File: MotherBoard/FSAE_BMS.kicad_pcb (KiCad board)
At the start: 4 copper layers, 139.7 x 127 mm, 209 parts, among them IC501 BQ79600PWRQ1, J201 Conn_ARM_SWD_TagConnect_TC2030, J202 DM3AT-SF-PEJM5_40_, J301 1376357-3, J302 Conn_01x04_Pin, J303 430450200, Q701 Q_NMOS_GDS, Q702 Q_NPN_BEC, Q703 Q_NPN_BEC, Q704 Q_NMOS_GDS, Q705 Q_NPN_BEC, Q706 Q_NMOS_GDS, Q708 Q_NPN_BEC, Q709 Q_NMOS_GDS, U201 STM32F205RBTx, U401 LMR51430, U402 LMR51430, U601 PTCAN1462DRQ1, U602 PTCAN1462DRQ1, Y201 16 Mhz

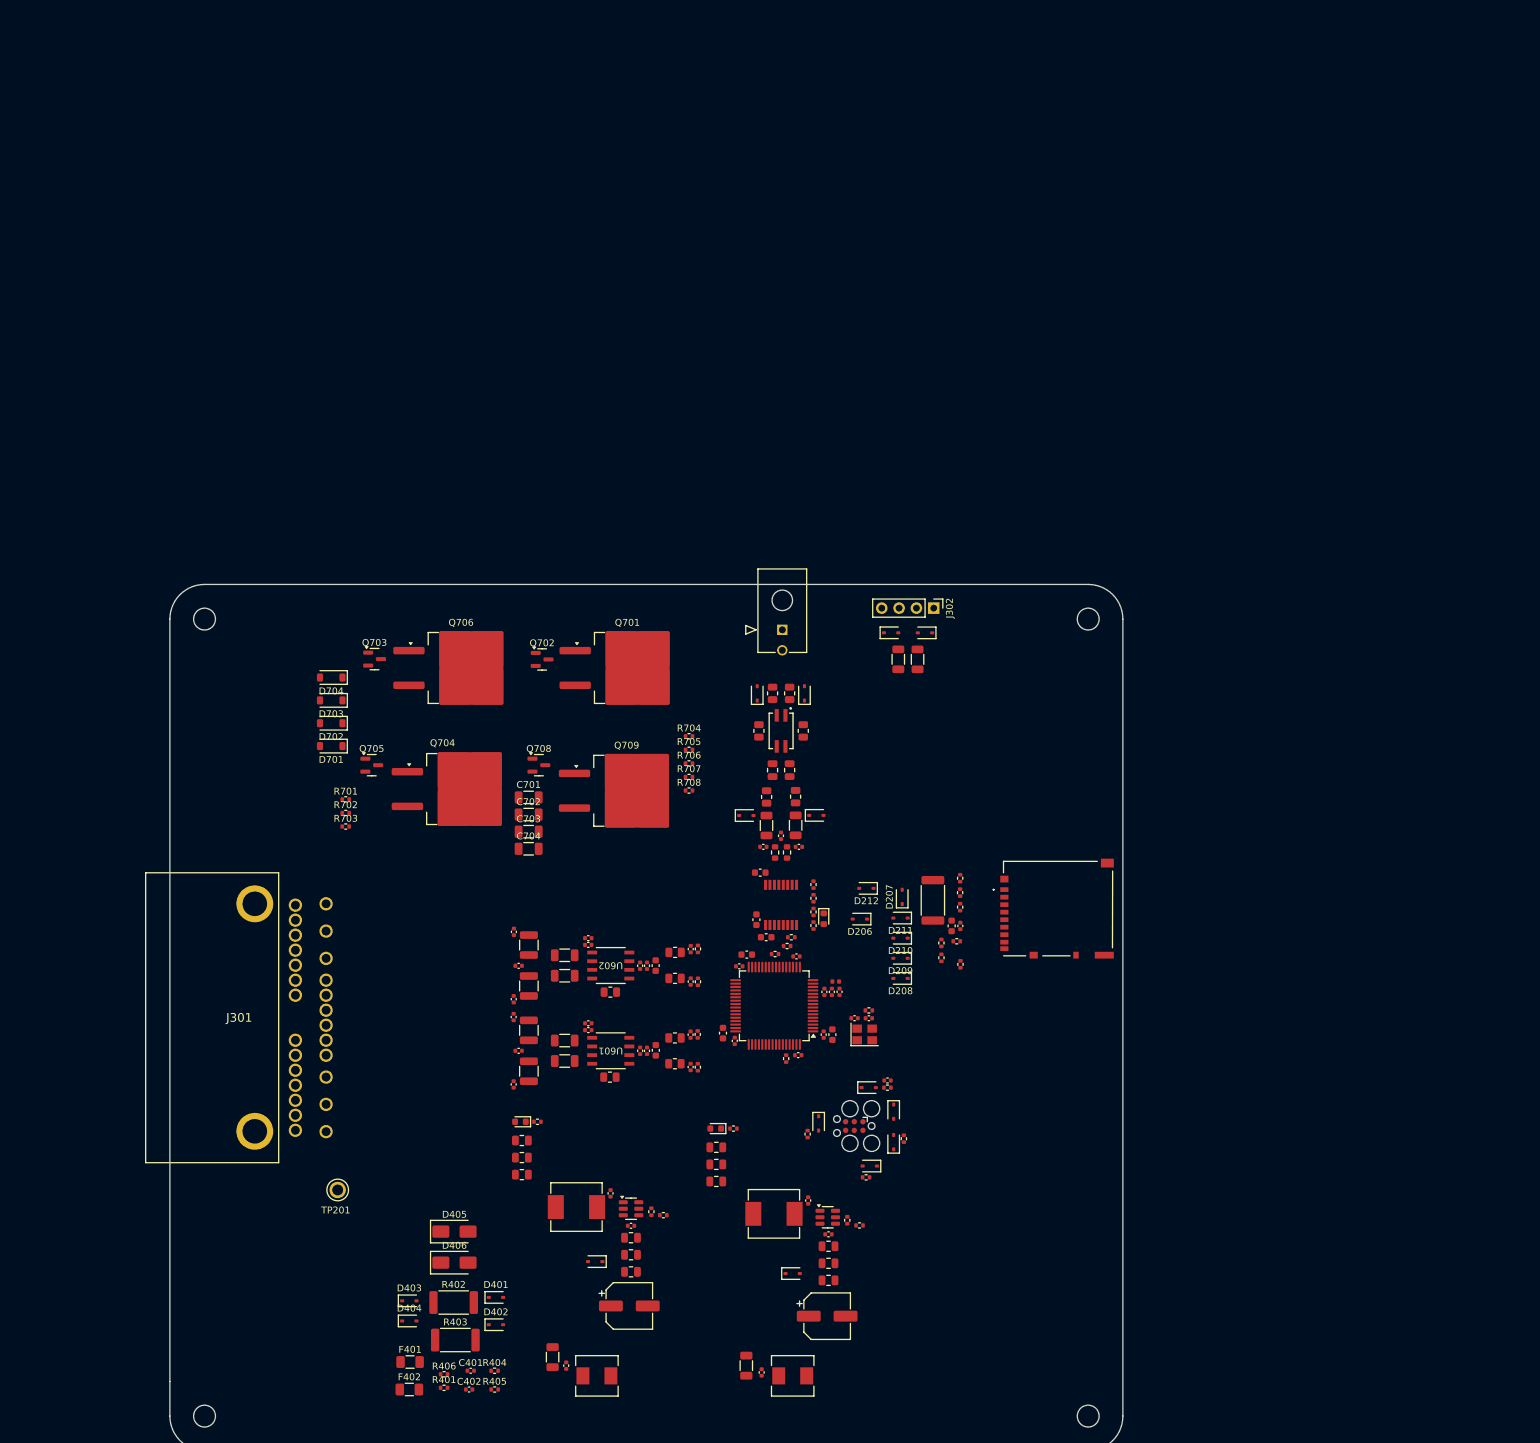
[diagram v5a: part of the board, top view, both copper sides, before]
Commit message: Layout complete for regulators and relay drivers
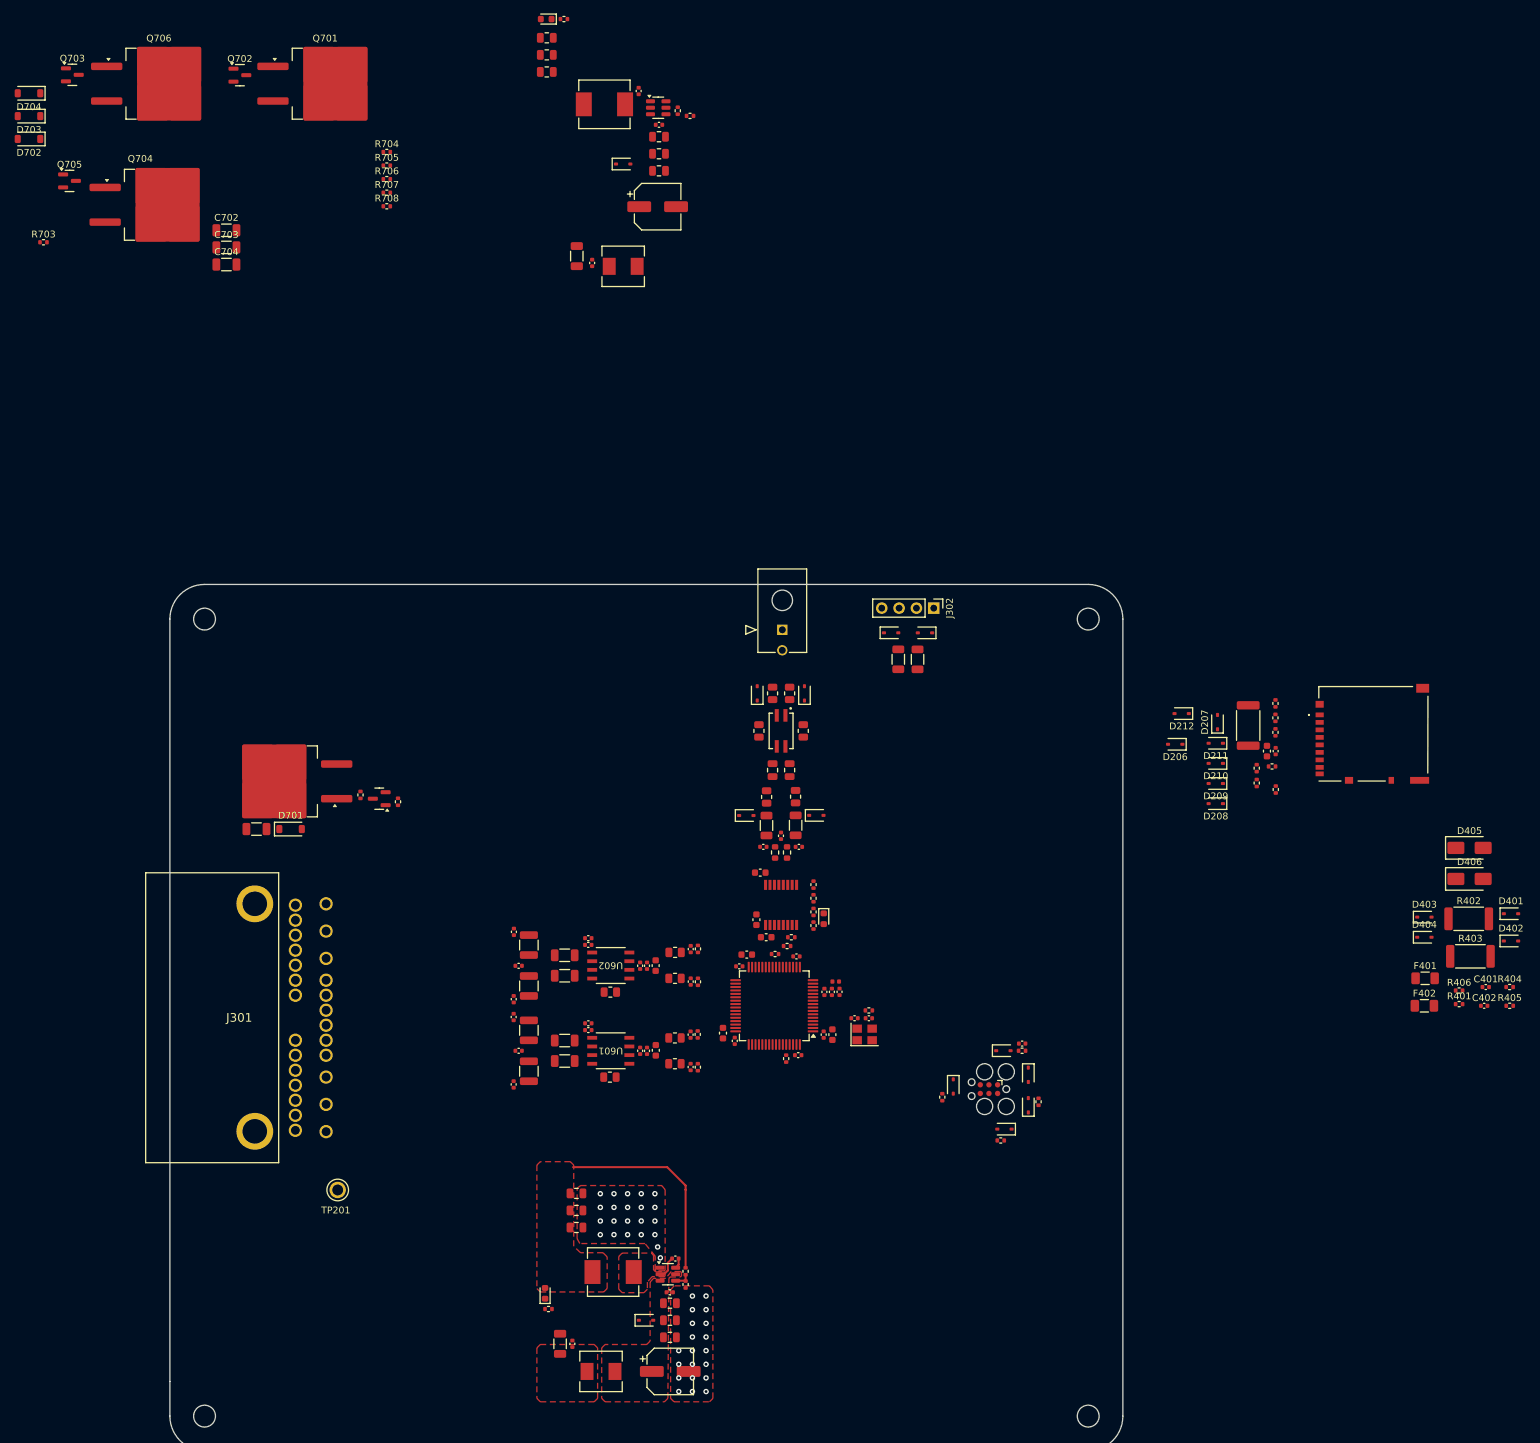
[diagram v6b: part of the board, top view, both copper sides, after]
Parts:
- moved C403 164.5 mm to (135.8, -22.8)
- moved C405 164.5 mm to (138.1, -21.8)
- moved C407 164.5 mm to (147.7, -30.0)
- moved C409 164.5 mm to (147.9, -40.2)
- moved C411 164.5 mm to (147.9, -35.2)
- moved C413 164.5 mm to (147.9, -37.8)
- moved C415 164.5 mm to (147.9, -42.0)
- moved C417 164.5 mm to (144.9, -47.0)
- moved C419 164.5 mm to (131.4, -49.8)
- moved C421 164.5 mm to (131.4, -52.2)
- moved C423 164.5 mm to (131.4, -54.8)
- moved D407 164.5 mm to (142.7, -36.2)
- moved D409 164.5 mm to (131.4, -57.5)
- moved L401 164.5 mm to (142.7, -21.2)
- moved L403 164.5 mm to (139.9, -45.0)
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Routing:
- net +5V: track 0.00 -> 29.7 mm
- net /PSU/BUCK_SW_5V: track 0.00 -> 3.37 mm
- net /PSU/BUCK_FB_5V: track 0.00 -> 2.41 mm
- net /PSU/CBOOT_5V: track 0.00 -> 1.53 mm
- net GND: vias 0 -> 42
- added copper zone on F.Cu, net +5V
- added copper zone on F.Cu, net /PSU/BUCK_SW_5V
- added copper zone on F.Cu, net GND
- added copper zone on In1.Cu, net GND
- added copper zone on In2.Cu, net GND
- added copper zone on F.Cu, net Net-(D408-A2)
- added copper zone on F.Cu, net VBUS

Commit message: Finished layout need to route
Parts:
- removed the D206 at (223.6, 48.8)
- removed the D207 at (229.8, 45.6)
- removed D210, D401, D402: D_TVS, Diode_SMD:D_SOD-323
- removed the R207 at (238.3, 42.8)
- removed the R208 at (238.3, 44.9)
- removed the R211 at (235.5, 54.5)
- added C502: 10n, Capacitor_SMD:C_0402_1005Metric, F.Cu at (135.5, 48.8)
- added C505: 100p, Capacitor_SMD:C_0402_1005Metric, F.Cu at (138.9, 51.3)
- added C506: 100p, Capacitor_SMD:C_0402_1005Metric, F.Cu at (138.9, 46.2)
- added C511: 2200p, Capacitor_SMD:C_0805_2012Metric, F.Cu at (125.6, 49.7)
- added C512: 2200p, Capacitor_SMD:C_0805_2012Metric, F.Cu at (125.6, 47.3)
- added D304: D_TVS, Diode_SMD:D_SOD-323, F.Cu at (114.2, 44.7)
- added D306: D_TVS, Diode_SMD:D_SOD-323, F.Cu at (114.2, 51.8)
- added D504: D_TVS, Diode_SMD:D_SOD-323, F.Cu at (134.0, 53.1)
- added D505: D_TVS, Diode_SMD:D_SOD-323, F.Cu at (134.0, 44.4)
- added G***: LOGO, LOGO, F.Cu at (123.2, 36.4)
- added J304: 430450200, molex_comm:CON_430450200_MOL, F.Cu at (103.4, 48.2)
- added L502: WE-SLM, WE-SLM:WE-SLM, F.Cu at (119.8, 48.2)
- added R504: 499, Resistor_SMD:R_0603_1608Metric, F.Cu at (138.1, 49.5)
- added R505: 499, Resistor_SMD:R_0603_1608Metric, F.Cu at (138.1, 48.0)
- added R512: 51, Resistor_SMD:R_1206_3216Metric, F.Cu at (134.0, 50.8)
- added R513: 51, Resistor_SMD:R_1206_3216Metric, F.Cu at (134.0, 46.6)
- added R518: 0R, Resistor_SMD:R_0805_2012Metric, F.Cu at (129.8, 50.8)
- added R519: 0R, Resistor_SMD:R_0805_2012Metric, F.Cu at (129.7, 46.6)
- added R522: 0R, Resistor_SMD:R_0805_2012Metric, F.Cu at (119.8, 51.5)
- added R523: 0R, Resistor_SMD:R_0805_2012Metric, F.Cu at (119.8, 44.9)
- added R526: 0R, Resistor_SMD:R_0805_2012Metric, F.Cu at (114.2, 49.5)
- added R527: 0R, Resistor_SMD:R_0805_2012Metric, F.Cu at (114.2, 47.0)
- moved D704 199.6 mm to (130.8, 138.2)
- moved Q708 187.7 mm to (131.5, 130.8)
- moved Q707 171.5 mm to (117.5, 128.3)
- moved C704 167.7 mm to (135.8, 138.2)
- moved D702 167.2 mm to (111.2, 117.8), turned to 90 degrees
- moved Q705 166.9 mm to (104.3, 118.8), turned to -90 degrees
- moved R707 160.1 mm to (114.9, 127.9), turned to 90 degrees
- moved R708 159.3 mm to (120.3, 128.8), turned to 90 degrees
- moved R411 157.1 mm to (180.0, 92.7)
- moved Q702 155.9 mm to (106.8, 105.3), turned to -90 degrees
- moved D409 155.6 mm to (179.5, 90.4), turned to 90 degrees
- moved C702 151.6 mm to (111.2, 122.7), turned to -90 degrees
- moved R705 145.9 mm to (106.3, 107.9)
- moved D703 144.4 mm to (111.1, 90.0), turned to 90 degrees
- moved C417 142.9 mm to (198.5, 85.5), turned to 180 degrees
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- renumbered C502 to C503, C503 to C504, C504 to C507, C505 to C508, C506 to C509, C507 to C510, C508 to C513, C606 to C604, C604 to C605, C607 to C606, C608 to C607, C615 to C608, C616 to C609, C605 to C610, C613 to C612, C619 to C613, C609 to C614, C610 to C615, C612 to C616, C614 to C617, C620 to C618, C617 to C619, C618 to C620, D208 to D206, D209 to D207, D211 to D208, D212 to D209, D304 to D303, D303 to D305, Q708 to Q701, Q709 to Q704, Q701 to Q705, Q704 to Q706, Q705 to Q707, Q706 to Q708, R205 to R203, R203 to R205, R209 to R207, R210 to R208, R212 to R209, R213 to R210, R214 to R211, R504 to R506, R505 to R507, R506 to R508, R507 to R509, R508 to R510, R509 to R511, R510 to R514, R511 to R515, R512 to R516, R513 to R517, R514 to R520, R515 to R521, R516 to R524, R517 to R525, R603 to R601, R606 to R602, R609 to R603, R610 to R606, R601 to R609, R602 to R610, R617 to R613, R618 to R614, R619 to R615, R620 to R616, R621 to R617, R622 to R618, R702 to R701, R703 to R702, R705 to R703, R701 to R704, R704 to R705
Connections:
- IC501 pad 10: unconnected-(IC501-COMLP-Pad10) -> /BQ79600/COMLP
- IC501 pad 11: unconnected-(IC501-COMLN-Pad11) -> /BQ79600/COMLN
- J202 pad 1: /MCU/SDIO_D2 -> unconnected-(J202-DAT2-Pad1)
- J202 pad 2: /MCU/SDIO_D3 -> unconnected-(J202-CD/DAT3-Pad2)
- J202 pad 8: /MCU/SDIO_D1 -> unconnected-(J202-DAT1-Pad8)
- U201 pad 40: /MCU/SDIO_D1 -> unconnected-(U201-PC9-Pad40)
- U201 pad 51: /MCU/SDIO_D2 -> unconnected-(U201-PC10-Pad51)
- U201 pad 52: /MCU/SDIO_D3 -> unconnected-(U201-PC11-Pad52)
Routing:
- net +3V3: track 0.00 -> 29.6 mm
- net /PSU/BUCK_SW_3V3: track 0.00 -> 2.78 mm
- net GND: vias 42 -> 84
- added copper zone on F.Cu, net +3V3
- added copper zone on F.Cu, net /PSU/BUCK_SW_3V3
- added copper zone on F.Cu, net Net-(D407-A2)
- removed copper zone on F.Cu, net VBUS
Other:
- board size 139.7 x 127 mm -> 110 x 115 mm

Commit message: Finished motherboard. Need to review BOM
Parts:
- removed the D208 at (180.8, 55.2)
- removed the D304 at (114.2, 44.7)
- removed D306: D_TVS, Diode_SMD:D_SOD-323
- removed the J303 at (103.3, 65.0)
- removed the R402 at (147.5, 64.9)
- removed the R403 at (151.8, 64.9)
- removed TP201: TestPoint, TestPoint:TP_5012
- added C301: 1u, Capacitor_SMD:C_0402_1005Metric, F.Cu at (159.9, 31.0)
- added D202: GREEN, LED_SMD:LED_0603_1608Metric, F.Cu at (171.9, 35.7)
- added D301: D_TVS, Diode_SMD:D_SOD-323, F.Cu at (148.6, 33.4)
- added D401: D_Zener, Diode_SMD:D_SOD-323, F.Cu at (140.9, 67.9)
- added D402: D_Zener, Diode_SMD:D_SOD-323, F.Cu at (140.8, 74.0)
- added F301: Fuse, Fuse:Fuse_0805_2012Metric, F.Cu at (143.4, 27.3)
- added F302: Fuse, Fuse:Fuse_0805_2012Metric, F.Cu at (132.0, 30.5)
- added J301: Conn_01x04_Pin, Connector_PinHeader_2.54mm:PinHeader_1x04_P2.54mm_Vertical, F.Cu at (154.7, 30.4)
- added J304: 430450200, molex_comm:CON_430450200_MOL, F.Cu at (98.3, 63.4)
- added J306: Conn_01x02_Pin, Connector_PinHeader_2.54mm:PinHeader_1x02_P2.54mm_Vertical, F.Cu at (167.3, 30.4)
- added R201: 1k, Resistor_SMD:R_0402_1005Metric, F.Cu at (173.2, 34.3)
- added R301: 22R, Resistor_SMD:R_1206_3216Metric, F.Cu at (153.8, 35.7)
- added R302: 22R, Resistor_SMD:R_1206_3216Metric, F.Cu at (148.2, 35.7)
- added R305: 2.2k, Resistor_SMD:R_1206_3216Metric, F.Cu at (161.6, 32.0)
- added R701: 10k, Resistor_SMD:R_0402_1005Metric, F.Cu at (107.5, 119.2)
- added R702: 10k, Resistor_SMD:R_0402_1005Metric, F.Cu at (132.4, 116.9)
- added R703: 10k, Resistor_SMD:R_0402_1005Metric, F.Cu at (189.9, 113.8)
- added R710: 10k, Resistor_SMD:R_0402_1005Metric, F.Cu at (112.5, 139.6)
- C508: footprint Capacitor_SMD:C_0603_1608Metric -> Capacitor_SMD:C_0402_1005Metric
- moved H104 104.8 mm to (95.3, 145.0)
- moved H103 100.4 mm to (200.3, 145.0)
- moved D703 95.4 mm to (197.1, 131.4), turned to 0 degrees
- moved C703 94.4 mm to (197.0, 133.9), turned to 0 degrees
- moved R709 93.8 mm to (191.0, 119.7)
- moved R706 93.8 mm to (192.0, 113.8)
- moved Q703 93.8 mm to (191.5, 116.5)
- moved Q706 93.8 mm to (188.9, 131.0)
- moved G*** 72.0 mm to (102.8, 105.4), turned to -90 degrees
- moved D305 58.0 mm to (164.5, 33.3)
- moved D303 53.0 mm to (153.3, 33.4)
- moved C702 46.5 mm to (157.6, 120.1), turned to 0 degrees
- moved D702 46.4 mm to (157.6, 117.6), turned to 0 degrees
- moved Q705 44.4 mm to (148.7, 117.8), turned to 0 degrees
- moved R708 32.3 mm to (137.8, 114.8), turned to -90 degrees
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- renumbered D202 to D203, D203 to D204, D204 to D205, D205 to D206, D206 to D207, D207 to D208, D301 to D302, D302 to D304, J301 to J303, J304 to J305, R201 to R202, R202 to R203, R203 to R204, R204 to R205, R205 to R206, R206 to R207, R207 to R208, R208 to R209, R209 to R210, R210 to R211, R211 to R212, R301 to R303, R302 to R304, R404 to R402, R405 to R403, R406 to R404, R407 to R405, R408 to R406, R409 to R407, R410 to R408, R411 to R409, R412 to R410, R701 to R704, R702 to R705, R703 to R706, R704 to R707, R705 to R708, R706 to R709, R707 to R711, R708 to R712
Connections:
- C401 pad 1: /PSU/READY_PWR_LV -> READY_PWR_LV_ISO
- C402 pad 1: /PSU/CHARGE_PWR_LV -> CHARGE_PWR_LV_ISO
- C505 pad 2: /BQ79600/COMLP -> /BQ79600/COMLN
- C506 pad 1: /BQ79600/COMLN -> /BQ79600/COMLP
- D303 pad 2: ISO_COMHP -> Net-(D303-A2)
- D305 pad 2: ISO_COMHN -> Net-(D305-A2)
- J302 pad 1: unconnected-(J302-Pin_1-Pad1) -> GND
- J302 pad 4: GND -> Net-(J302-Pin_4)
- R401 pad 1: /PSU/READY_PWR_LV -> READY_PWR_LV_ISO
- R402 pad 2: /PSU/READY_PWR_LV -> READY_PWR_LV_ISO
- R403 pad 2: /PSU/CHARGE_PWR_LV -> CHARGE_PWR_LV_ISO
- R404 pad 1: /PSU/CHARGE_PWR_LV -> CHARGE_PWR_LV_ISO
- R504 pad 1: /BQ79600/COMLP -> /BQ79600/COMLN
- R505 pad 2: /BQ79600/COMLN -> /BQ79600/COMLP
- R512 pad 1: /BQ79600/COMLP -> /BQ79600/COMLN
- R513 pad 1: /BQ79600/COMLN -> /BQ79600/COMLP
- R526 pad 2: ISO_COMLP -> ISO_COMLN
- R527 pad 2: ISO_COMLN -> ISO_COMLP
- R707 pad 1: +12V -> VBUS
- R708 pad 1: +12V -> VBUS
- R709 pad 1: +12V -> VBUS
- R712 pad 1: +12V -> VBUS
- U201 pad 10: unconnected-(U201-PC2-Pad10) -> /MCU/TEST_LED
- U201 pad 14: unconnected-(U201-PA0-Pad14) -> UART4_TX
- U201 pad 15: unconnected-(U201-PA1-Pad15) -> UART4_RX
- U201 pad 2: /MCU/SDIO_DET -> unconnected-(U201-PC13-Pad2)
- U201 pad 9: unconnected-(U201-PC1-Pad9) -> ADC_IN
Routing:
- net +3V3: track 29.6 -> 350.2 mm, vias 0 -> 14
- net CHARGE_PWR_LV_ISO: track 0.00 -> 290.9 mm, vias 0 -> 2
- net +5V: track 29.4 -> 293.7 mm, vias 0 -> 4
- net READY_PWR_LV_ISO: track 0.00 -> 262.5 mm, vias 0 -> 2
- net DISCHARGE_EN_LV: track 0.00 -> 129.4 mm, vias 0 -> 2
- net FAN_EN_LV: track 0.00 -> 117.7 mm, vias 0 -> 2
- net CHARGE_EN_LV: track 0.00 -> 101.9 mm, vias 0 -> 2
- net GND: track 0.00 -> 86.6 mm, vias 84 -> 993
- net CHARGE_SAFE_LV: track 0.00 -> 81.9 mm, vias 0 -> 2
- net VBUS: track 0.00 -> 67.8 mm
- net ISO_CAN2+: track 0.00 -> 46.8 mm, vias 0 -> 1
- net ISO_CAN1-: track 0.00 -> 46.4 mm, vias 0 -> 1
- net ISO_CAN2-: track 0.00 -> 46.3 mm, vias 0 -> 1
- net ISO_CAN1+: track 0.00 -> 45.9 mm, vias 0 -> 1
- net ADC_IN: track 0.00 -> 33.1 mm, vias 0 -> 2
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- added copper zone on F.Cu, net +3.3VP
- added copper zone on F.Cu, net CHARGE_EN_HV
- added copper zone on F.Cu, net CHARGE_SAFE_HV
- added copper zone on F.Cu, net DISCHARGE_EN_HV
- added copper zone on F.Cu, net FAN_EN_HV
- added copper zone on F.Cu, net VBUS
- added copper zone on F.Cu, net VDDA
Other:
- board size 110 x 115 mm -> 115 x 125 mm
- board text added: "120Ω"
- board text added: "12V MAX"
- board text added: "3.3V"
- board text added: "500mA MAX"
- board text added: "5V"
- board text added: "ADC"
- board text added: "CAN1"
- board text added: "CAN2"
- board text added: "CHARGE EN"
- board text added: "CHARGER SAFETY"
- board text added: "COMHN"
- board text added: "COMHP"
- board text added: "COMLN"
- board text added: "COMLP"
- board text added: "DEBUG"
- board text added: "DISCHARGE EN"
- board text added: "FAN EN"
- board text added: "GND"
- board text added: "IN"
- board text added: "INSERT MICRO SD"
- board text added: "M3"
- board text added: "READY POWER CHARGE POWER"
- board text added: "RX"
- board text added: "SENTRY BMS"
- board text added: "SWD"
- board text added: "TX"
- board text added: "UART1"
- board text added: "UART2"
- board text added: "https://github.com/JacobParent7/FSAE_LSU_BMS"
